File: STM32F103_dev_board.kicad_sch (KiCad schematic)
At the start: 35 parts, among them IC1 TLV70233DBVR, IC2 FT232RNL-REEL, J1 Conn_ARM_JTAG_SWD_20, J2 Conn_01x20_Pin, J3 Conn_01x20_Pin, J4 Conn_02x03_Odd_Even, J6 USB4800-03-A, U1 STM32F103RBTx, Y1 8MHz, Y2 Crystal_GND23

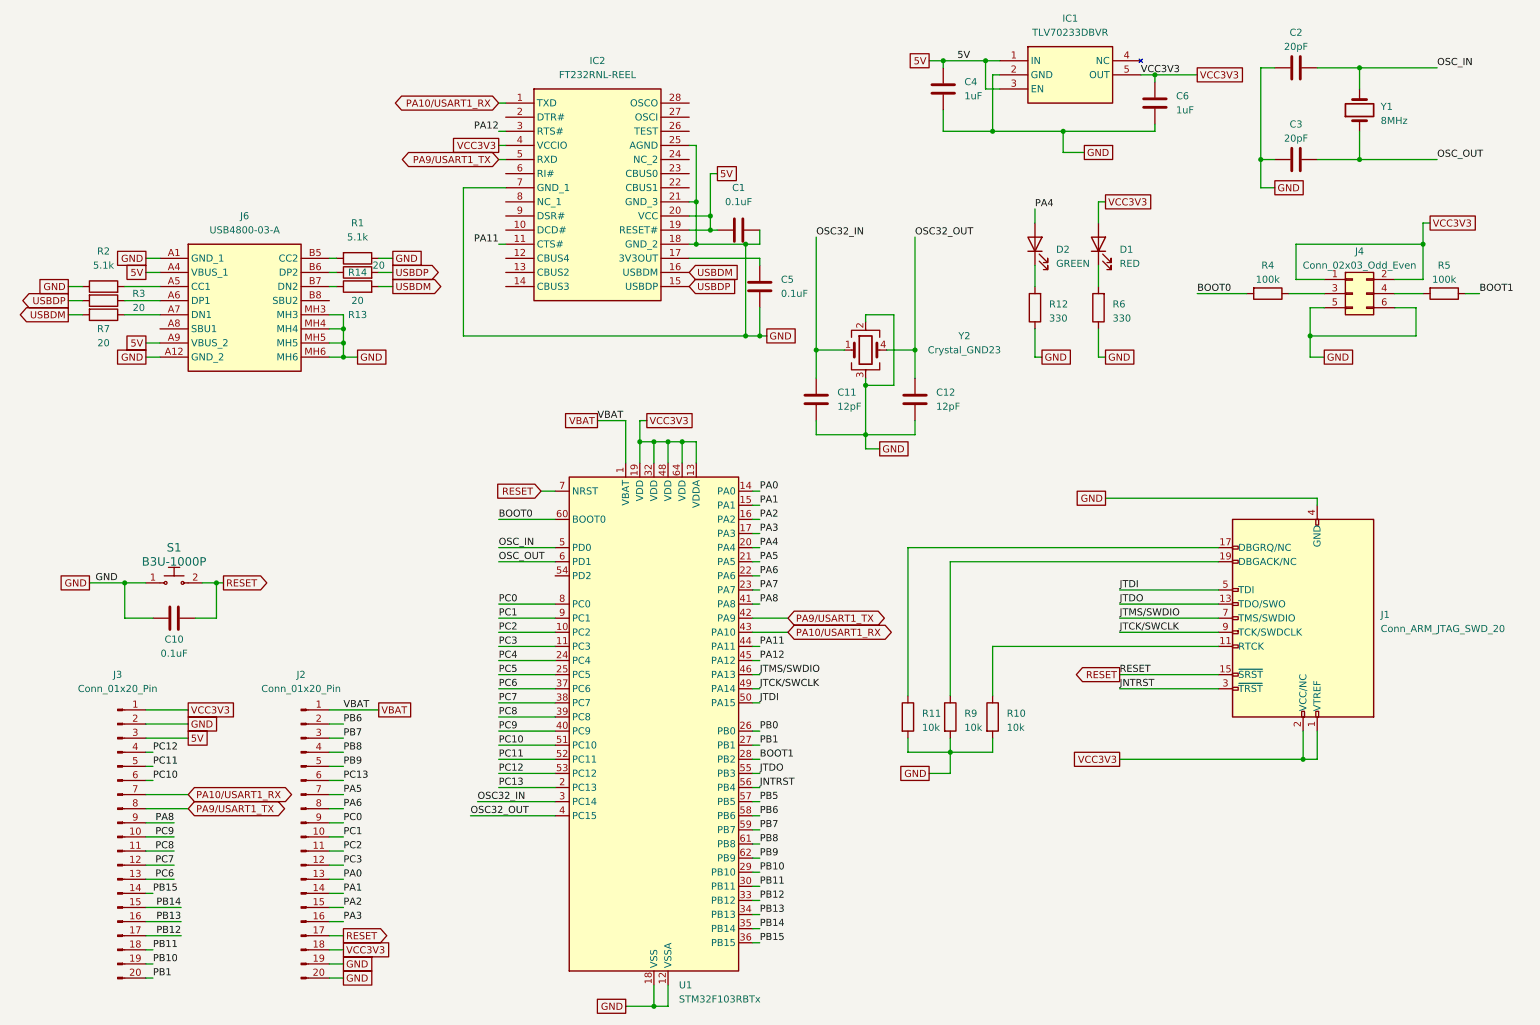
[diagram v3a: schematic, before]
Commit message: Changed net labels into global labels
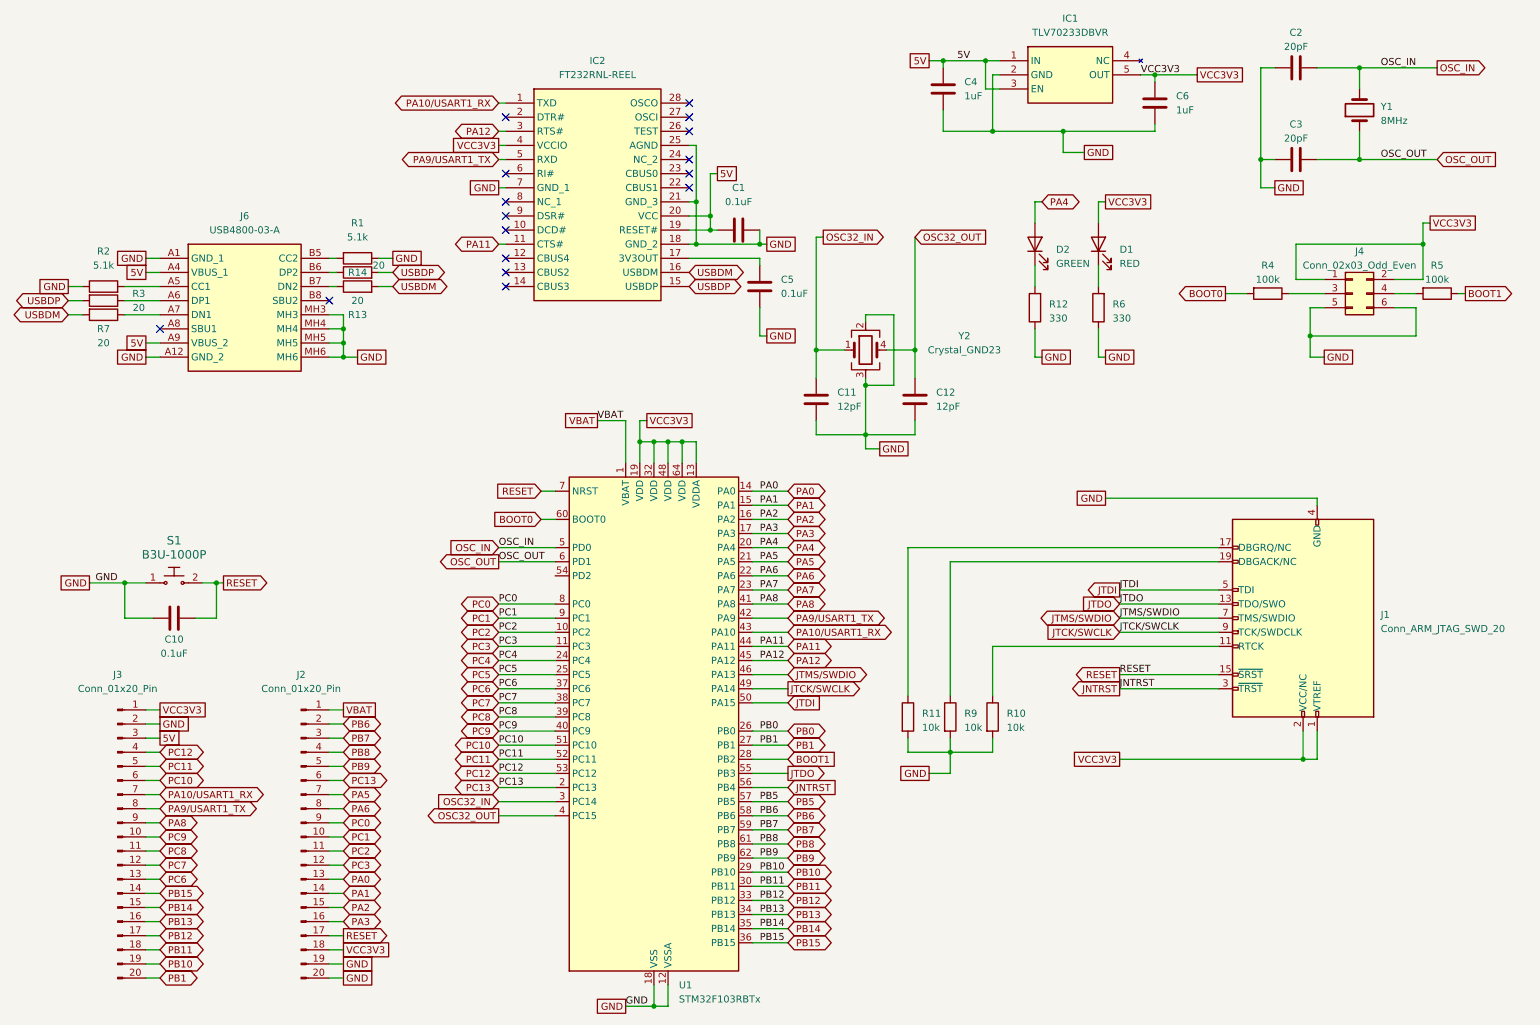
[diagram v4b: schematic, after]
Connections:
- no-connect marks 0 -> 16
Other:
- moved on the sheet: R5

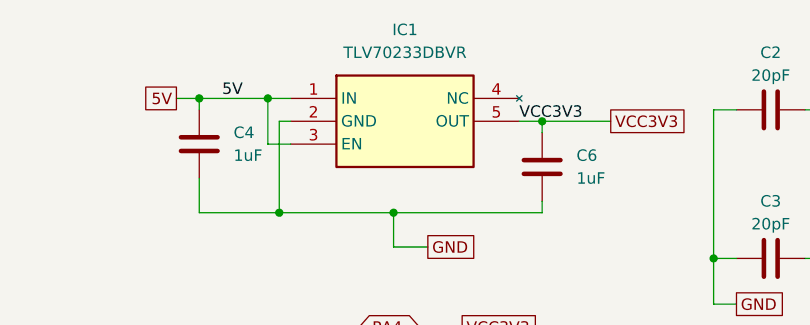
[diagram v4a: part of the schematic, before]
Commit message: changed LDO to TLV75733PDBVR
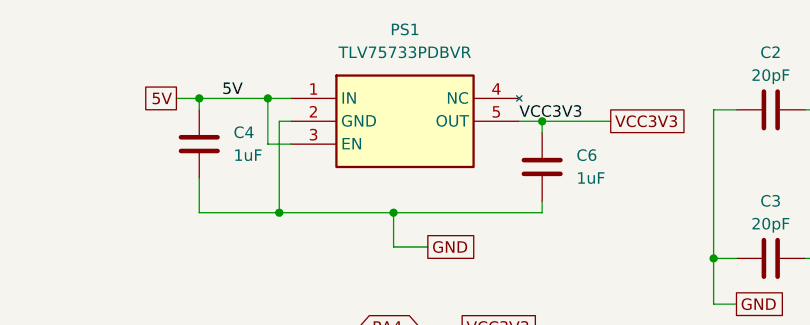
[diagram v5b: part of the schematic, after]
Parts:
- removed IC1: TLV70233DBVR, SOT95P280X145-5N, symbol SamacSys_Parts:TLV70233DBVR
- added PS1: TLV75733PDBVR, SOT95P280X145-5N, symbol SamacSys_Parts:TLV75733PDBVR
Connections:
- net 5V: now also PS1.1 (IN), PS1.3 (EN)
- net GND: now also PS1.2 (GND)
- net VCC3V3: now also PS1.5 (OUT)
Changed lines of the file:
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@@
   (title_block
     (title "STM32F103RBT6 Dev Board")
-    (date "2023-10-13")
-    (rev "1.1.2")
+    (date "2023-11-17")
+    (rev "1.1.3")
   )
   (junction (at 201.93 35.56) (diameter 0) (color 0 0 0 0)
@@
     )
   )
-  (symbol (lib_id "SamacSys_Parts:TLV70233DBVR") (at 190.5 22.86 0) (unit 1)
-    (in_bom yes) (on_board yes) (dnp no) (fields_autoplaced)
-    (property "Reference" "IC1" (at 203.2 15.24 0)
-      (effects (font (size 1.27 1.27)))
-    )
-    (property "Value" "TLV70233DBVR" (at 203.2 17.78 0)
-      (effects (font (size 1.27 1.27)))
-    )
-    (property "Footprint" "SOT95P280X145-5N" (at 212.09 117.78 0)
-      (effects (font (size 1.27 1.27)) (justify left top) hide)
-    )
-    (property "Datasheet" "http://www.ti.com/lit/gpn/tlv702" (at 212.09 217.78 0)
-      (effects (font (size 1.27 1.27)) (justify left top) hide)
-    )
-    (property "Height" "1.45" (at 212.09 417.78 0)
-      (effects (font (size 1.27 1.27)) (justify left top) hide)
-    )
-    (property "Mouser Part Number" "595-TLV70233DBVR" (at 212.09 517.78 0)
-      (effects (font (size 1.27 1.27)) (justify left top) hide)
-    )
-    (property "Mouser Price/Stock" "https://www.mouser.co.uk/ProductDetail/Texas-Instruments/TLV70233DBVR?qs=zQ2yIHQ6k3wiHrD0NUI05Q%3D%3D" (at 212.09 617.78 0)
-      (effects (font (size 1.27 1.27)) (justify left top) hide)
-    )
-    (property "Manufacturer_Name" "Texas Instruments" (at 212.09 717.78 0)
-      (effects (font (size 1.27 1.27)) (justify left top) hide)
-    )
-    (property "Manufacturer_Part_Number" "TLV70233DBVR" (at 212.09 817.78 0)
-      (effects (font (size 1.27 1.27)) (justify left top) hide)
-    )
-    (pin "1")
-    (pin "2")
-    (pin "3")
-    (pin "4")
-    (pin "5")
-    (instances
-      (project "STM32F103_dev_board"
-        (path "/93ed7a92-70c4-4662-9ca1-0ce61928fd3a"
-          (reference "IC1") (unit 1)
-        )
-      )
-    )
-  )
   (symbol (lib_id "Device:C") (at 218.44 30.48 180) (unit 1)
     (in_bom yes) (on_board yes) (dnp no) (fields_autoplaced)
@@
         )
       )
+    )
+  )
+  (symbol (lib_id "SamacSys_Parts:TLV75733PDBVR") (at 190.5 22.86 0) (unit 1)
+    (in_bom yes) (on_board yes) (dnp no) (fields_autoplaced)
+    (property "Reference" "PS1" (at 203.2 15.24 0)
+      (effects (font (size 1.27 1.27)))
+    )
+    (property "Value" "TLV75733PDBVR" (at 203.2 17.78 0)
+      (effects (font (size 1.27 1.27)))
+    )
+    (property "Footprint" "SOT95P280X145-5N" (at 212.09 117.78 0)
+      (effects (font (size 1.27 1.27)) (justify left top) hide)
+    )
+    (property "Datasheet" "http://www.ti.com/lit/gpn/tlv757p" (at 212.09 217.78 0)
+      (effects (font (size 1.27 1.27)) (justify left top) hide)
+    )
+    (property "Height" "1.45" (at 212.09 417.78 0)
+      (effects (font (size 1.27 1.27)) (justify left top) hide)
+    )
+    (property "Manufacturer_Name" "Texas Instruments" (at 212.09 517.78 0)
+      (effects (font (size 1.27 1.27)) (justify left top) hide)
+    )
+    (property "Manufacturer_Part_Number" "TLV75733PDBVR" (at 212.09 617.78 0)
+      (effects (font (size 1.27 1.27)) (justify left top) hide)
+    )
+    (property "Mouser Part Number" "595-TLV75733PDBVR" (at 212.09 717.78 0)
+      (effects (font (size 1.27 1.27)) (justify left top) hide)
+    )
+    (property "Mouser Price/Stock" "https://www.mouser.co.uk/ProductDetail/Texas-Instruments/TLV75733PDBVR?qs=y6ZabgHbY%252BwAAzSntTW34w%3D%3D" (at 212.09 817.78 0)
+      (effects (font (size 1.27 1.27)) (justify left top) hide)
+    )
+    (property "Arrow Part Number" "TLV75733PDBVR" (at 212.09 917.78 0)
+      (effects (font (size 1.27 1.27)) (justify left top) hide)
+    )
+    (property "Arrow Price/Stock" "https://www.arrow.com/en/products/tlv75733pdbvr/texas-instruments?region=nac" (at 212.09 1017.78 0)
+      (effects (font (size 1.27 1.27)) (justify left top) hide)
+    )
+    (pin "2")
+    (pin "3")
+    (pin "5")
+    (pin "1")
+    (pin "4")
+    (instances
+      (project "STM32F103_dev_board"
+        (path "/93ed7a92-70c4-4662-9ca1-0ce61928fd3a"
+          (reference "PS1") (unit 1)
+        )
+      )

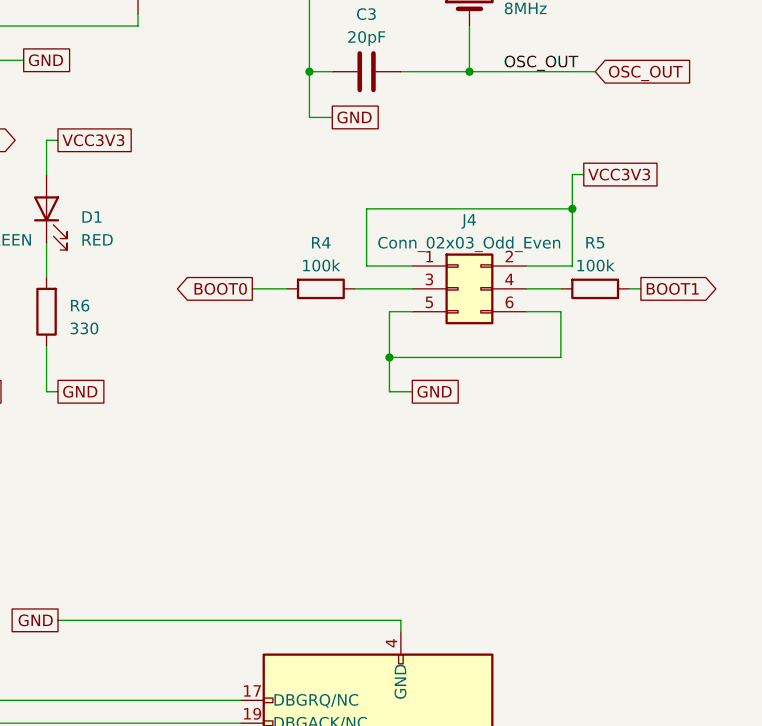
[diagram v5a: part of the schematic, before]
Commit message: Changed boot mode selector to SPDT slide switch
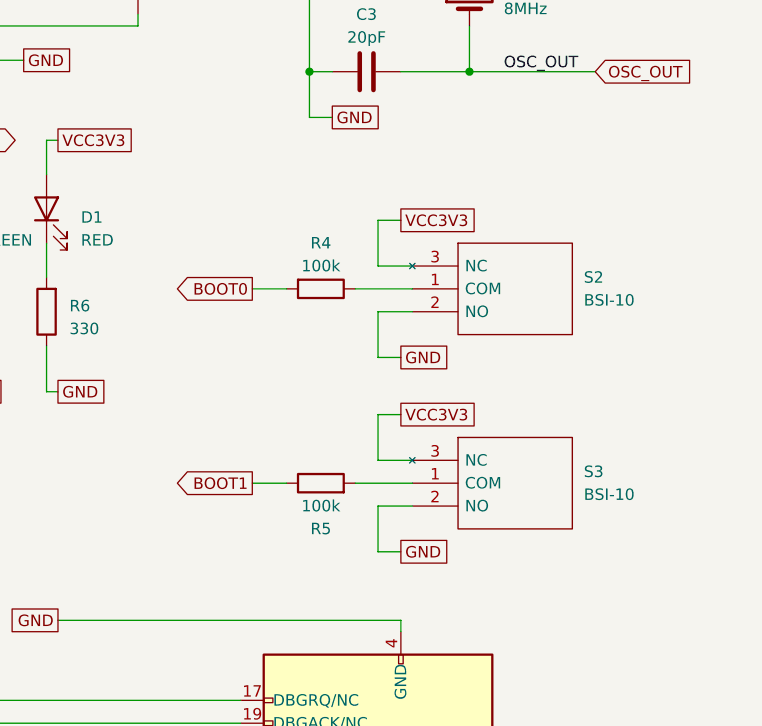
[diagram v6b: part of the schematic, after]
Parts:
- removed J4: Conn_02x03_Odd_Even, Connector_PinHeader_2.54mm:PinHeader_2x03_P2.54mm_Vertical, symbol Connector_Generic:Conn_02x03_Odd_Even
- added S2, S3: BSI-10, BSI10, symbol SamacSys_Parts:BSI-10
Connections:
- net GND: now also S2.2 (NO), S3.2 (NO)
- net VCC3V3: now also S2.3 (NC), S3.3 (NC)
- net at R4.1: now also S2.1 (COM)
- net at R5.2: now also S3.1 (COM)

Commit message: Minor changes
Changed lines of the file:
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@@
     )
   )
-  (symbol (lib_id "SamacSys_Parts:BSI-10") (at 248.92 62.23 0) (unit 1)
+  (symbol (lib_name "BSI-10_1") (lib_id "SamacSys_Parts:BSI-10") (at 248.92 62.23 0) (unit 1)
     (in_bom yes) (on_board yes) (dnp no) (fields_autoplaced)
     (property "Reference" "S2" (at 267.97 63.5 0)
